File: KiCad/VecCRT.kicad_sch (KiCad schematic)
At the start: 86 parts, among them J1 RaspiGPIO, J2 K2, J3 Conn_01x03, J4 Conn_01x06, J5 Conn_01x03, J6 Conn_01x06, J7 K2, J8 Conn_01x03, K1 SchEin, Q1 2N7000, Q10 2N7000, Q2 2N7002, Q3 2N7002, Q4 2N7000, Q5 2N7002, Q6 2N7002, Q7 2N7000, Q9 2N7000, U1 MCP4822, U2 4066, U3 4066, U4 TL072, U5 TL072, U6 4011, U7 40106, U8 4011, X1 OPL820-OC

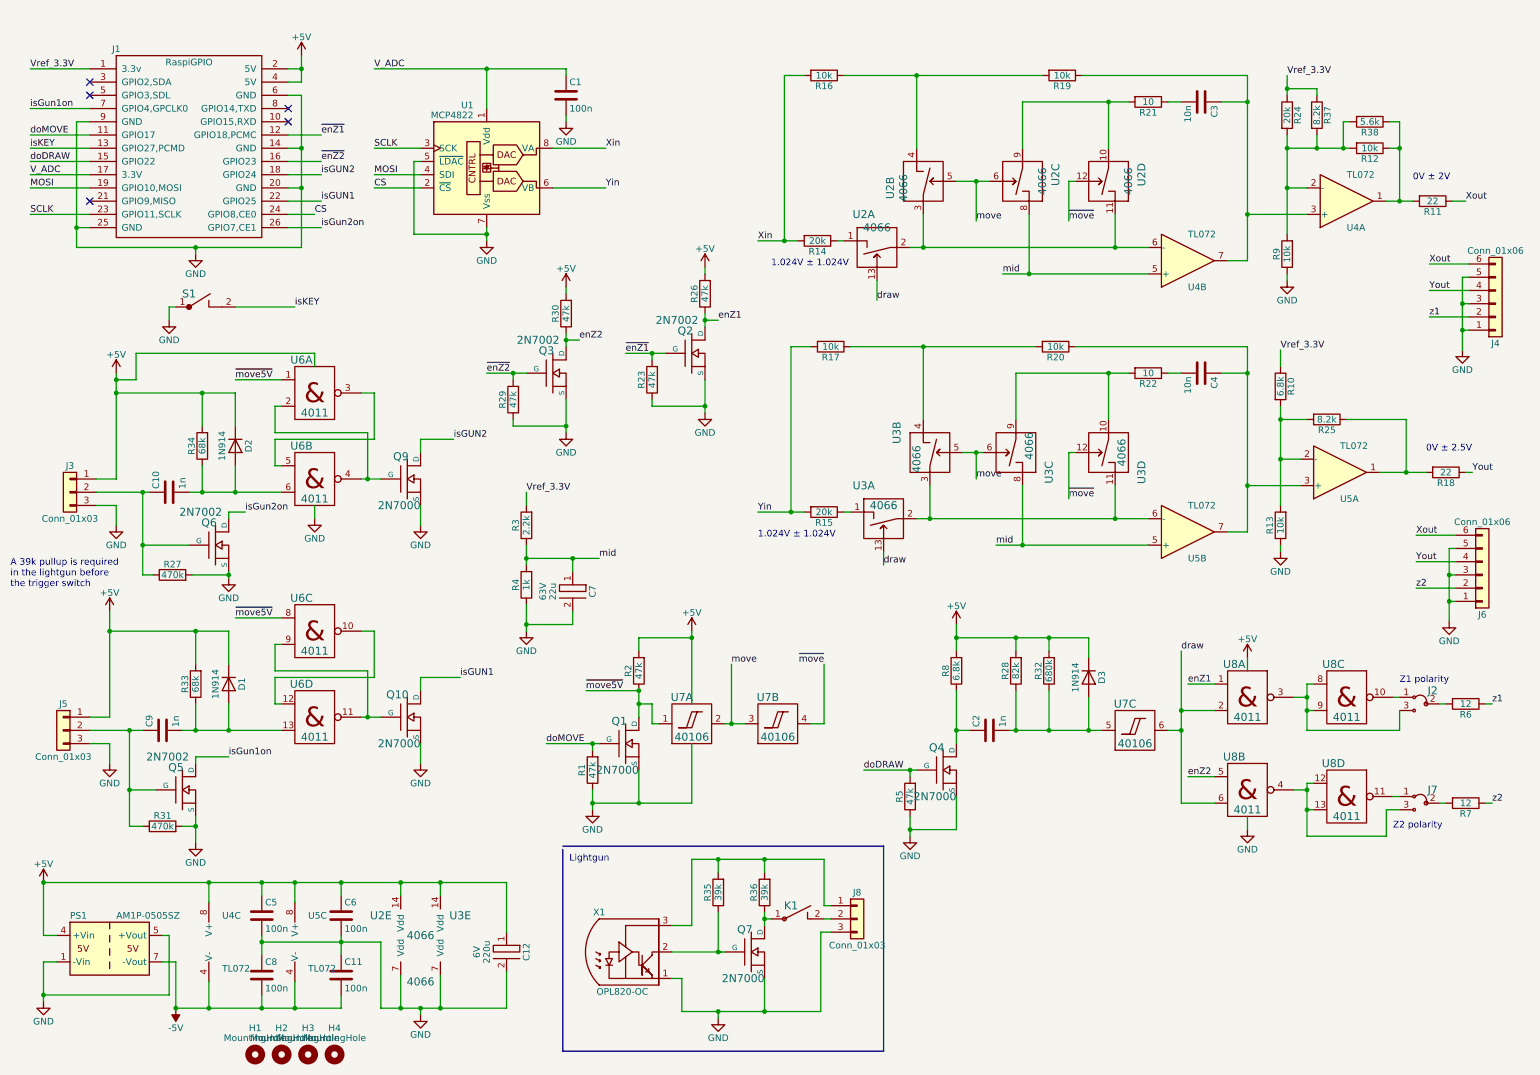
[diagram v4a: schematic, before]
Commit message: Schematics for 1.0a
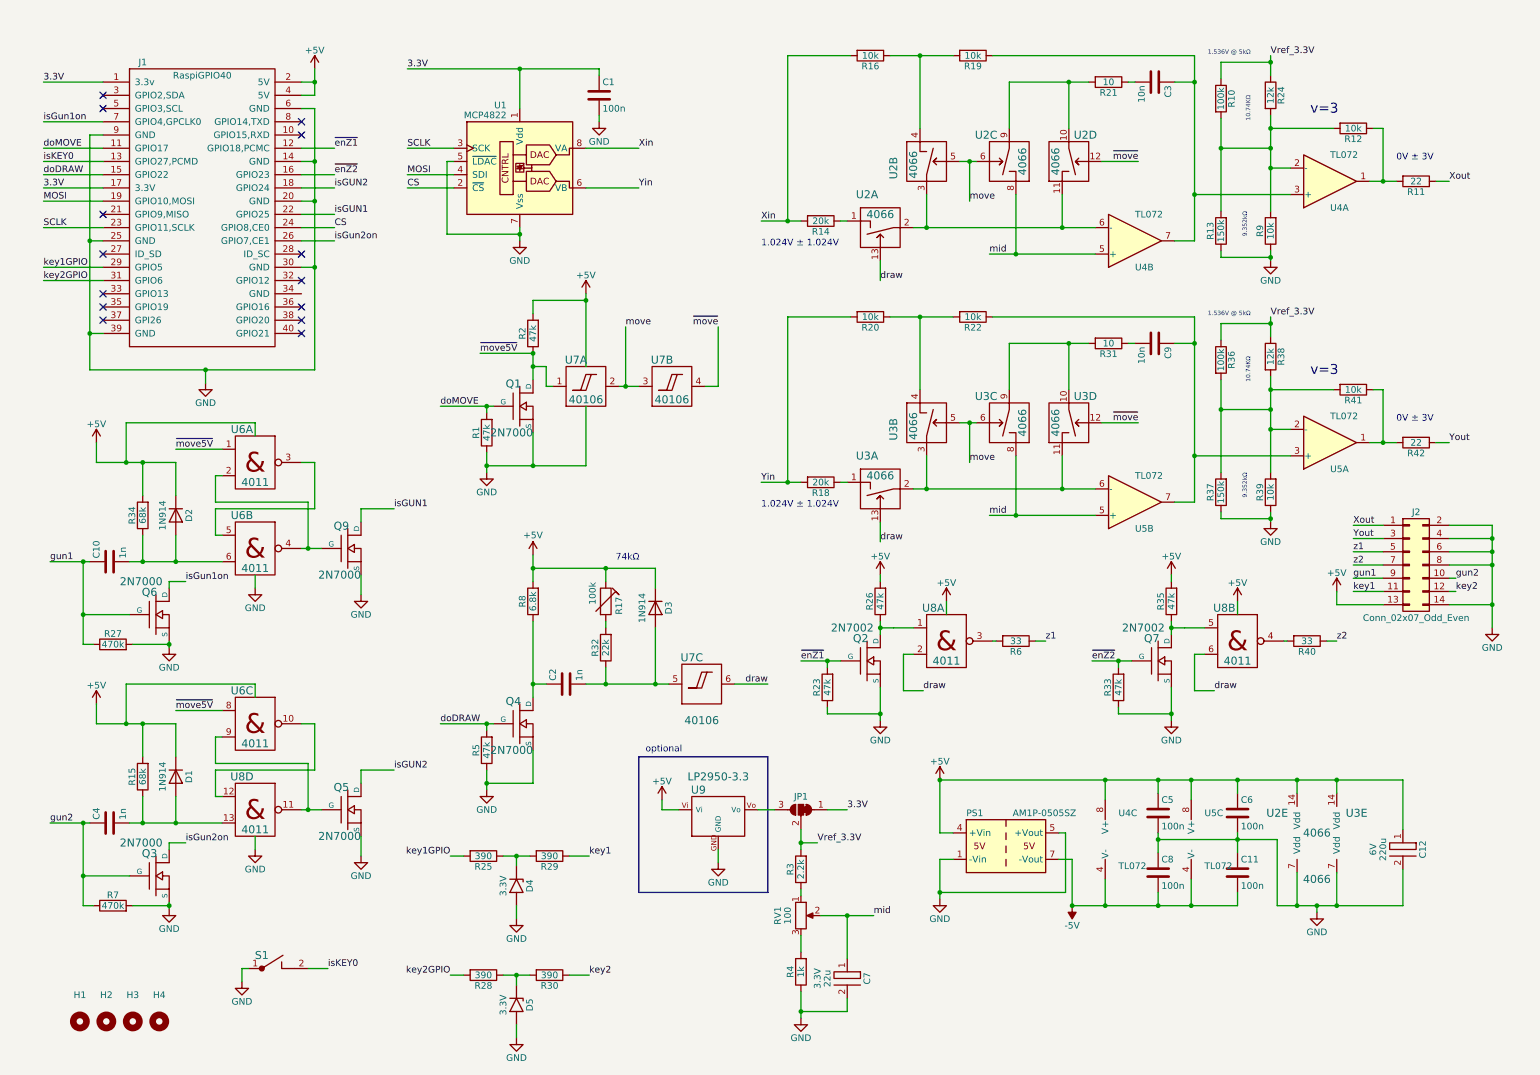
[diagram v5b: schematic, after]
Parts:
- removed J1: RaspiGPIO, Connector_PinHeader_2.54mm:PinHeader_2x13_P2.54mm_Vertical, symbol VecCRT-rescue:RaspiGPIO-rg
- removed J2, J7: K2, RG:Pins_3, symbol rg:K2
- removed J3, J5, J8: Conn_01x03, RG:PSS_3, symbol Connector_Generic:Conn_01x03
- removed J4, J6: Conn_01x06, RG:PSS_6, symbol Connector_Generic:Conn_01x06
- removed K1: SchEin, PINHEAD1-2, symbol rg:SchEin
- removed Q10, Q7: 2N7000, RG:FETsgd_inline, symbol rg:BS170
- removed Q5: 2N7002, RG:SOT-23_GDS, symbol rg:2N7002
- removed R17: 10k, RG:R4-2, symbol Device:R
- removed unit 4 of U6
- removed unit 3 of U8
- removed X1: OPL820-OC, symbol rg:OPL820-OC
- added D4, D5: 3.3V, symbol rg:D_Zener
- added J1: RaspiGPIO40, Connector_PinHeader_2.54mm:PinHeader_2x20_P2.54mm_Vertical, symbol rg:RaspiGPIO40
- added J2: Conn_02x07_Odd_Even, symbol Connector_Generic:Conn_02x07_Odd_Even
- added JP1: SolderJumper_3_Bridged12, symbol Jumper:SolderJumper_3_Bridged12
- added Q5: 2N7000, RG:FETsgd_inline, symbol rg:BS170
- added Q7: 2N7002, RG:SOT-23_GDS, symbol rg:2N7002
- added R17: 100k, symbol Device:R_Trim
- added R39, R41: 10k, RG:R4-2, symbol Device:R
- added R40: 33, RG:R4-2, symbol Device:R
- added R42: 22, RG:R4-2, symbol Device:R
- added RV1: 100, symbol Device:R_Potentiometer
- added U9: LP2950-3.3, symbol rg:78L05
- C4: value 10n -> 1n
- C7: Voltage 63V -> 3.3V
- C9: value 1n -> 10n
- Q3, Q6: value 2N7002 -> 2N7000; footprint RG:SOT-23_GDS -> RG:TO-92SGD
- R10: value 6.8k -> 100k
- R13: value 10k -> 150k
- R15: value 20k -> 68k
- R18: value 22 -> 20k
- R22: value 10 -> 10k
- R24: value 20k -> 12k
- R25: value 8.2k -> 390
- R28: value 82k -> 390
- R29, R30: value 47k -> 390; footprint RG:SM-1206B -> RG:R4-2
- R31: value 470k -> 10; footprint RG:SM-1206B -> RG:R4-2
- R32: value 680k -> 22k
- R33: value 68k -> 47k; footprint RG:R4-2 -> RG:SM-1206B
- R35: value 39k -> 47k; footprint RG:R4-2 -> RG:SM-1206B
- R36: value 39k -> 100k
- R37: value 8.2k -> 150k
- R38: value 5.6k -> 12k
- R6: value 12 -> 33
- R7: value 12 -> 470k; footprint RG:R4-2 -> RG:SM-1206B
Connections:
- net +5V: now also R15.2, R35.2, J1.2 (5V), J1.4 (5V), J2.13 (Pin_13), R17.1, U9.Vi; no longer R28.2, R30.2, R32.2, R33.2
- net CS: now also J1.24 (GPIO8,CE0)
- net GND: now also R33.1, R37.1, R7.2, D4.2 (A), D5.2 (A), J1.14 (GND), J1.20 (GND), J1.25 (GND), J1.30 (GND), J1.39 (GND), J1.6 (GND), J1.9 (GND), J2.14 (Pin_14), J2.2 (Pin_2), J2.4 (Pin_4), J2.6 (Pin_6), J2.8 (Pin_8), Q5.S, Q7.S, R39.1, U9.GND; no longer R29.1, R31.2
- net MOSI: now also J1.19 (GPIO10,MOSI)
- net SCLK: now also J1.23 (GPIO11,SCLK)
- net Vref_3.3V: now also R36.1, R38.1, JP1.2 (C); no longer R37.1
- net Xout: now also J2.1 (Pin_1)
- net Yin: now also R18.2, R20.2; no longer R15.2
- net Yout: now also J2.3 (Pin_3), R42.1; no longer R18.1
- net doDRAW: now also J1.15 (GPIO22)
- net doMOVE: now also J1.11 (GPIO17)
- net isGUN1: now also Q9.D, J1.22 (GPIO25)
- net isGUN2: now also J1.18 (GPIO24), Q5.D; no longer Q9.D
- net isGun1on: now also Q6.D, J1.7 (GPIO4,GPCLK0)
- net isGun2on: now also Q3.D, J1.26 (GPIO7,CE1); no longer Q6.D
- net mid: now also RV1.2; no longer R3.1, R4.2
- net z1: now also J2.5 (Pin_5)
- net z2: now also J2.7 (Pin_7), R40.1; no longer R7.1
- net ~{enZ1}: now also J1.12 (GPIO18,PCMC)
- net ~{enZ2}: now also R33.2, J1.16 (GPIO23), Q7.G; no longer Q3.G, R29.2
- net at R11.2, R12.1, U4.1: no longer R38.1
- net at R12.2, R24.2, R9.2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: now also R10.2, R13.2; no longer R37.2, R38.2
- net at U5.3 (+), U5.7: now also C9.1, R22.1; no longer C4.1, R20.1
- net gun1: now reaches C10.1, Q6.G, R27.1
- net gun1: now also J2.9 (Pin_9)
- net at R31.1: now also C9.2; no longer C9.1
- net at C2.2, D3.2 (A), R32.1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: no longer R28.1
- net at U3.4: now also R20.1, R22.2; no longer R20.2
- net at U3.10, U3.9: now also R31.2; no longer R22.2
- net at R15.1: now also C4.2, D1.2 (A), U8.13; no longer U3.1
- net at R6.2: now also U8.3
- net at U6.10: now also U8.12
- net at U6.9: now also U8.11, Q5.G
- net at R35.1: now also U8.5, Q7.D
- net at R36.2: now also R37.2, R38.2, U5.2 (-), R39.2, R41.2; no longer R35.2
- net V_ADC renamed 3.3V
- net 3.3V: now also J1.1 (3.3v), J1.17 (3.3V), JP1.1 (A)
- net enZ1: no longer names the net of Q2.D, R26.1, U8.1
- removed net enZ2: Q3.D, R30.1, U8.5
- net isKEY renamed isKEY0
- net isKEY0: now also J1.13 (GPIO27,PCMD)
- new net: R17.2, R32.2
- new net: R3.1, RV1.1
- new net: R4.2, RV1.3
- new net: R41.1, R42.2, U5.1
- new net: D5.1 (K), R28.1, R30.2
- new net: D4.1 (K), R25.1, R29.2
- new net: R40.2, U8.4
- new net: JP1.3 (B), U9.Vo
- new net: R18.1, U3.1
- new net gun2: C4.1, J2.10 (Pin_10), Q3.G, R7.1
- new net key1: J2.11 (Pin_11), R29.1
- new net key1GPIO: J1.29 (GPIO5), R25.2
- new net key2: J2.12 (Pin_12), R30.1
- new net key2GPIO: J1.31 (GPIO6), R28.2
- no-connect marks 5 -> 14
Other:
- note added: "0V ± 3V"
- note added: "1.536V @ 5kΩ"
- note added: "10.74KΩ"
- note added: "74kΩ"
- note added: "9.352kΩ"
- note added: "optional"
- note added: "v=3"
- note removed: "0V ± 2.5V"
- note removed: "0V ± 2V"
- note removed: "A 39k pullup is required in the lightgun before the trigger switch"
- note removed: "Lightgun"
- note removed: "Z1 polarity"
- note removed: "Z2 polarity"
- moved on the sheet: C1, C10, C11, C12, C2, C3, C5, C6, C7, C8, D2, D3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

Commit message: 1.0c: moved I²C to own bus
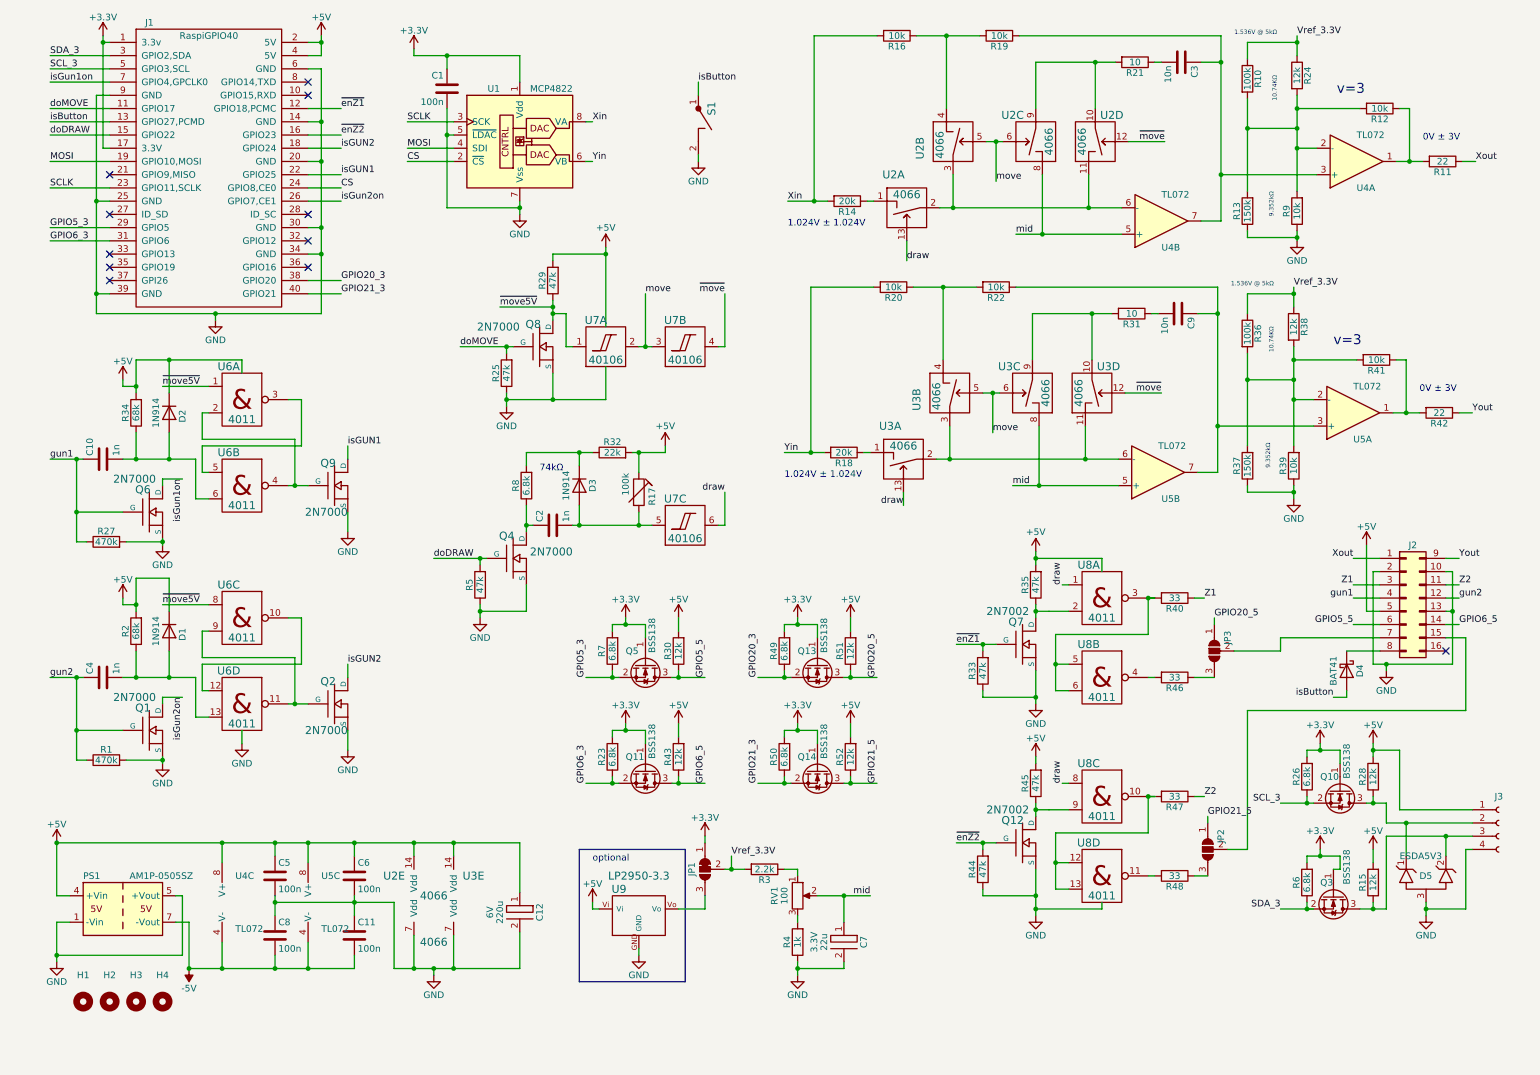
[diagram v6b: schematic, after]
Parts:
- removed D4, D5: 3.3V, symbol rg:D_Zener
- removed J2: Conn_02x07_Odd_Even, symbol Connector_Generic:Conn_02x07_Odd_Even
- removed Q1, Q5: 2N7000, RG:FETsgd_inline, symbol rg:BS170
- removed Q2: 2N7002, RG:SOT-23_GDS, symbol rg:2N7002
- removed Q3: 2N7000, RG:TO-92SGD, symbol rg:2N7002
- added D4: BAT41, Diode_THT:D_DO-35_SOD27_P7.62mm_Horizontal, symbol Diode:BAT41
- added D5: ESDA5V3, Package_TO_SOT_SMD:SOT-23_Handsoldering, symbol rg:ESDA5V3
- added J2: Conn_02x08_Top_Bottom, symbol Connector_Generic:Conn_02x08_Top_Bottom
- added J3: Conn_01x04_Female, symbol Connector:Conn_01x04_Female
- added JP2, JP3: SolderJumper_3_Open, symbol Jumper:SolderJumper_3_Open
- added Q1: 2N7000, RG:TO-92SGD, symbol rg:2N7002
- added Q10, Q11, Q13, Q14, Q3, Q5: BSS138, Package_TO_SOT_SMD:SOT-23, symbol Transistor_FET:BSS138
- added Q12: 2N7002, RG:SOT-23_GDS, symbol rg:2N7002
- added Q2, Q8: 2N7000, RG:FETsgd_inline, symbol rg:BS170
- added R43, R51, R52: 12k, RG:R4-2, symbol Device:R
- added R44, R45: 47k, RG:SM-1206B, symbol Device:R
- added R46, R47, R48: 33, RG:R4-2, symbol Device:R
- added R49, R50: 6.8k, RG:R4-2, symbol Device:R
- added unit 4 of U6
- added unit 3 of U8
- R1: value 47k -> 470k
- R15: value 68k -> 12k
- R2: value 47k -> 68k; footprint RG:SM-1206B -> RG:R4-2
- R23, R26: value 47k -> 6.8k; footprint RG:SM-1206B -> RG:R4-2
- R25, R29: value 390 -> 47k; footprint RG:R4-2 -> (none)
- R28, R30: value 390 -> 12k
- R6: value 33 -> 6.8k
- R7: value 470k -> 6.8k; footprint RG:SM-1206B -> RG:R4-2
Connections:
- net key1 is gone; now on net ~{move5V}: R29.1
- net z1 is gone; now on net SDA_3: R6.1
- net +5V: now also R28.2, R29.2, R30.2, R32.2, J2.5 (Pin_5), J3.1 (Pin_1), R43.2, R45.2, R51.2, R52.2, U6.14 (VDD), U8.14 (VDD); no longer D3.1 (K), R26.2, R8.2
- net GND: now also J1.34 (GND), R1.2, R25.1, S1.2, D5.3 (A), J2.10 (Pin_10), J2.13 (Pin_13), J2.2 (Pin_2), J3.4 (Pin_4), Q1.S, Q12.S, Q2.S, Q8.S, R44.1, U6.7 (VSS), U8.7 (VSS); no longer R1.1, R23.1, R7.2, S1.1
- net Xout: now also J2.1 (Pin_1)
- net Yout: now also J2.9 (Pin_9)
- net doMOVE: now also R25.2, Q8.G; no longer R1.2
- net draw: now also U8.1, U8.8; no longer U8.2, U8.6
- net gun1: now also J2.4 (Pin_4)
- net gun2: now also R1.1, J2.12 (Pin_12), Q1.G; no longer R7.1
- net isGUN2: now also Q2.D
- net isGun2on: now also Q1.D
- net ~{enZ1}: now also Q7.G, R33.2; no longer R23.2
- net ~{enZ2}: now also Q12.G, R44.2; no longer Q7.G, R33.2
- net ~{move5V}: now also Q8.D; no longer R2.1
- net at C2.2, D3.2 (A), U7.5: now also R17.2; no longer R32.1
- net SCL_3: now reaches R26.1
- net SCL_3: now also J1.5 (GPIO3,SCL), Q10.2 (S); no longer U8.1
- net at U8.3: now also R40.2, U8.5, U8.6; no longer R6.2
- net at R28.1: now also D5.1 (K1), J3.2 (Pin_2), Q10.3 (D); no longer R30.2
- net at U6.9: now also Q2.G, U6.11; no longer U8.11
- net at U8.4: now also R46.2; no longer R40.2
- net at Q7.D, R35.1: now also U8.2; no longer U8.5
- net at U8.12: now also U8.13, R47.2, U8.10; no longer U6.10
- net at C4.2, D1.2 (A): now also R2.1, U6.13; no longer R15.1, U8.13
- net SDA_3: now reaches J1.3 (GPIO2,SDA)
- net SDA_3: now also Q3.2 (S)
- net GPIO20_3: now reaches J1.38 (GPIO20)
- net GPIO20_3: now also Q13.2 (S), R49.1
- net GPIO21_3: now reaches J1.40 (GPIO21)
- net GPIO21_3: now also Q14.2 (S), R50.1
- net 3.3V renamed +3.3V
- net +3.3V: now also R23.2, R26.2, R6.2, R7.2, Q10.1 (G), Q11.1 (G), Q13.1 (G), Q14.1 (G), Q3.1 (G), Q5.1 (G), R49.2, R50.2
- net isKEY0 renamed isButton
- net isButton: now also S1.1, D4.2 (A); no longer S1.2
- net key1GPIO renamed GPIO5_3
- net GPIO5_3: now also R7.1, Q5.2 (S); no longer R25.2
- net key2 renamed GPIO5_5
- net GPIO5_5: now also J2.6 (Pin_6), Q5.3 (D)
- net key2GPIO renamed GPIO6_3
- net GPIO6_3: now also R23.1, Q11.2 (S); no longer R28.2
- net z2 renamed Z1
- net Z1: now also J2.3 (Pin_3)
- new net: D3.1 (K), R32.1, R8.2
- new net: J2.7 (Pin_7), JP3.2 (C)
- new net: JP3.3 (B), R46.1
- new net: D5.2 (K2), J3.3 (Pin_3), Q3.3 (D), R15.1
- new net: Q12.D, R45.1, U8.9
- new net: U6.10, U6.12
- new net: J2.15 (Pin_15), JP2.2 (C)
- new net: D4.1 (K), J2.8 (Pin_8)
- new net: JP2.3 (B), R48.1
- new net: R48.2, U8.11
- new net GPIO20_5: JP3.1 (A), Q13.3 (D), R51.1
- new net GPIO21_5: JP2.1 (A), Q14.3 (D), R52.1
- new net GPIO6_5: J2.14 (Pin_14), Q11.3 (D), R43.1
- new net Z2: J2.11 (Pin_11), R47.1
- no-connect marks 14 -> 11
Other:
- moved on the sheet: C1, C10, C11, C12, C2, C3, C5, C6, C7, C8, C9, D2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
